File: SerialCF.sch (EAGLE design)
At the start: 17 parts, among them IC1 XR-16C550P, T1 BC547, T2 BC547

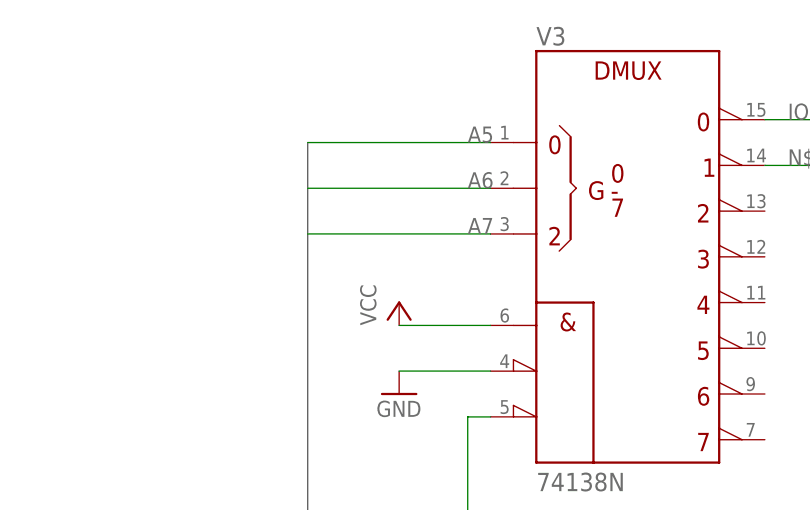
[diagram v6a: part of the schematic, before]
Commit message: Use upper Bits to Address IO devices.
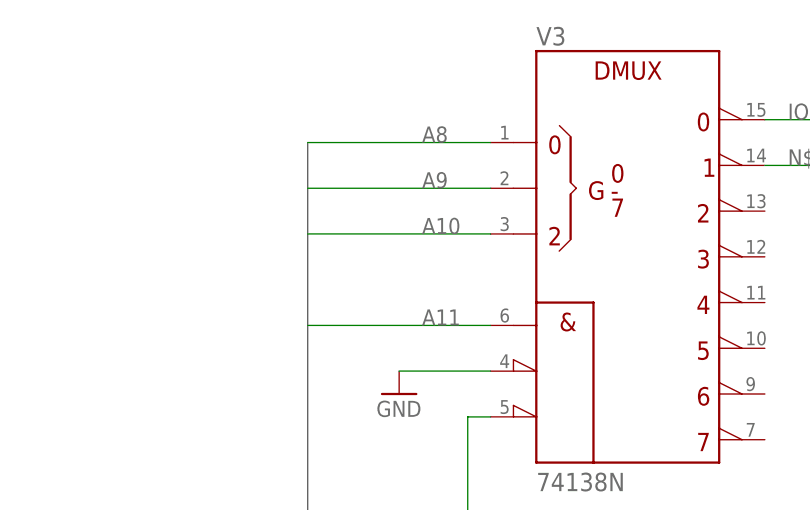
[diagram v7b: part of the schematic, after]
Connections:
- net A10: now also V31.C
- net A11: now also V31.G1
- net A5: no longer V31.A
- net A6: no longer V31.B
- net A7: no longer V31.C
- net A8: now also V31.A
- net A9: now also V31.B
- net VCC: no longer V31.G1
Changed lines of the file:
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@@
 <part name="GND9" library="supply1" deviceset="GND" device=""/>
 <part name="V3" library="74ttl-din" deviceset="74*138" device="N"/>
-<part name="P+12" library="supply1" deviceset="VCC" device=""/>
 <part name="GND13" library="supply1" deviceset="GND" device=""/>
 <part name="T2" library="transistor" deviceset="BC547" device=""/>
@@
 <instance part="V3" gate="/+UB" x="17.78" y="96.52"/>
 <instance part="V3" gate="/-UB" x="17.78" y="86.36"/>
-<instance part="P+12" gate="VCC" x="86.36" y="132.08"/>
 <instance part="GND13" gate="1" x="86.36" y="121.92"/>
 <instance part="T2" gate="G$1" x="111.76" y="-15.24"/>
@@
 <pinref part="JP1" gate="A" pin="A7"/>
 <wire x1="66.04" y1="48.26" x2="76.2" y2="48.26" width="0.1524" layer="91"/>
-</segment>
-<segment>
-<pinref part="V3" gate="1" pin="C"/>
-<wire x1="96.52" y1="139.7" x2="76.2" y2="139.7" width="0.1524" layer="91"/>
-<label x="93.98" y="139.7" size="1.778" layer="95"/>
 </segment>
 </net>
@@
 <pinref part="P+1" gate="VCC" pin="VCC"/>
 <pinref part="V3" gate="/+UB" pin="+UB"/>
-</segment>
-<segment>
-<pinref part="P+12" gate="VCC" pin="VCC"/>
-<pinref part="V3" gate="1" pin="G1"/>
-<wire x1="86.36" y1="129.54" x2="96.52" y2="129.54" width="0.1524" layer="91"/>
 </segment>
 <segment>
@@
 <wire x1="66.04" y1="53.34" x2="76.2" y2="53.34" width="0.1524" layer="91"/>
 </segment>
-<segment>
-<pinref part="V3" gate="1" pin="A"/>
-<wire x1="96.52" y1="149.86" x2="76.2" y2="149.86" width="0.1524" layer="91"/>
-<label x="93.98" y="149.86" size="1.778" layer="95"/>
-</segment>
 </net>
 <net name="A6" class="0">
@@
 <wire x1="266.7" y1="68.58" x2="266.7" y2="73.66" width="0.1524" layer="91"/>
 </segment>
-<segment>
-<pinref part="V3" gate="1" pin="B"/>
-<wire x1="96.52" y1="144.78" x2="76.2" y2="144.78" width="0.1524" layer="91"/>
-<label x="93.98" y="144.78" size="1.778" layer="95"/>
-</segment>
 </net>
 <net name="A8" class="0">
@@
 <wire x1="66.04" y1="45.72" x2="76.2" y2="45.72" width="0.1524" layer="91"/>
 </segment>
+<segment>
+<pinref part="V3" gate="1" pin="A"/>
+<wire x1="76.2" y1="149.86" x2="96.52" y2="149.86" width="0.1524" layer="91"/>
+<label x="88.9" y="149.86" size="1.778" layer="95"/>
+</segment>
 </net>
 <net name="A9" class="0">
@@
 <wire x1="66.04" y1="43.18" x2="76.2" y2="43.18" width="0.1524" layer="91"/>
 </segment>
+<segment>
+<pinref part="V3" gate="1" pin="B"/>
+<wire x1="76.2" y1="144.78" x2="96.52" y2="144.78" width="0.1524" layer="91"/>
+<label x="88.9" y="144.78" size="1.778" layer="95"/>
+</segment>
 </net>
 <net name="A10" class="0">
@@
 <wire x1="66.04" y1="40.64" x2="76.2" y2="40.64" width="0.1524" layer="91"/>
 </segment>
+<segment>
+<pinref part="V3" gate="1" pin="C"/>
+<wire x1="76.2" y1="139.7" x2="96.52" y2="139.7" width="0.1524" layer="91"/>
+<label x="88.9" y="139.7" size="1.778" layer="95"/>
+</segment>
 </net>
 <net name="A11" class="0">
@@
 <wire x1="66.04" y1="38.1" x2="76.2" y2="38.1" width="0.1524" layer="91"/>
 </segment>
-</net>
+<segment>
+<pinref part="V3" gate="1" pin="G1"/>
+<wire x1="76.2" y1="129.54" x2="96.52" y2="129.54" width="0.1524" layer="91"/>
+<label x="88.9" y="129.54" size="1.778" layer="95"/>
+</segment>
+</net>

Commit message: Use LS version for serialCF
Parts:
- removed V3: 74138N, 74ttl-din:74138N
- added IC2: 74LS138N, 74xx-eu:74LS138N
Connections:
- net A10: now also IC2A.C; no longer V31.C
- net A11: now also IC2A.G1; no longer V31.G1
- net A8: now also IC2A.A; no longer V31.A
- net A9: now also IC2A.B; no longer V31.B
- net GND: now also IC2P.GND; no longer V3/-UB.-UB, V31.!G2A
- net IOCS1: no longer V31.Y0
- net N$4: now also IC2A.Y1; no longer V31.Y1
- net N$5: no longer V31.!G2B
- net VCC: now also IC2P.VCC; no longer V3/+UB.+UB
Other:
- note removed: "A7 = 0 A6 = 0"
- note removed: "A7 = 0 A6 = 1"
- moved on the sheet: C4
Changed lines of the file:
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@@
 <part name="P+11" library="supply1" deviceset="VCC" device=""/>
 <part name="GND9" library="supply1" deviceset="GND" device=""/>
-<part name="V3" library="74ttl-din" deviceset="74*138" device="N"/>
 <part name="GND13" library="supply1" deviceset="GND" device=""/>
 <part name="T2" library="transistor" deviceset="BC547" device=""/>
@@
 <part name="P+13" library="supply1" deviceset="VCC" device=""/>
 <part name="GND14" library="supply1" deviceset="GND" device=""/>
+<part name="IC2" library="74xx-eu" deviceset="74*138" device="N" technology="LS"/>
 </parts>
 <sheets>
 <sheet>
 <plain>
-<text x="157.48" y="55.88" size="1.778" layer="91">A7 = 0
-A6 = 1</text>
-<text x="281.94" y="53.34" size="1.778" layer="91">A7 = 0
-A6 = 0</text>
 </plain>
 <instances>
@@
 <instance part="P+7" gate="VCC" x="314.96" y="43.18"/>
 <instance part="GND6" gate="1" x="314.96" y="30.48"/>
-<instance part="C4" gate="G$1" x="223.52" y="111.76"/>
-<instance part="P+11" gate="VCC" x="223.52" y="116.84"/>
-<instance part="GND9" gate="1" x="223.52" y="104.14"/>
-<instance part="V3" gate="1" x="111.76" y="137.16"/>
-<instance part="V3" gate="/+UB" x="17.78" y="96.52"/>
-<instance part="V3" gate="/-UB" x="17.78" y="86.36"/>
-<instance part="GND13" gate="1" x="86.36" y="121.92"/>
+<instance part="C4" gate="G$1" x="297.18" y="63.5"/>
+<instance part="P+11" gate="VCC" x="297.18" y="68.58"/>
+<instance part="GND9" gate="1" x="297.18" y="55.88"/>
+<instance part="GND13" gate="1" x="86.36" y="132.08"/>
 <instance part="T2" gate="G$1" x="111.76" y="-15.24"/>
 <instance part="R5" gate="G$1" x="101.6" y="-15.24"/>
@@
 <instance part="P+13" gate="VCC" x="114.3" y="2.54"/>
 <instance part="GND14" gate="1" x="114.3" y="-22.86"/>
+<instance part="IC2" gate="A" x="111.76" y="142.24"/>
+<instance part="IC2" gate="P" x="17.78" y="91.44"/>
 </instances>
 <busses>
@@
 </segment>
 <segment>
-<pinref part="P+1" gate="VCC" pin="VCC"/>
-<pinref part="V3" gate="/+UB" pin="+UB"/>
-</segment>
-<segment>
 <pinref part="R6" gate="G$1" pin="2"/>
 <pinref part="P+13" gate="VCC" pin="VCC"/>
+</segment>
+<segment>
+<pinref part="P+1" gate="VCC" pin="VCC"/>
+<pinref part="IC2" gate="P" pin="VCC"/>
 </segment>
 </net>
@@
 </segment>
 <segment>
-<pinref part="GND3" gate="1" pin="GND"/>
-<pinref part="V3" gate="/-UB" pin="-UB"/>
-</segment>
-<segment>
 <pinref part="T2" gate="G$1" pin="E"/>
 <pinref part="GND14" gate="1" pin="GND"/>
 </segment>
 <segment>
-<pinref part="V3" gate="1" pin="!G2A"/>
 <pinref part="GND13" gate="1" pin="GND"/>
-<wire x1="96.52" y1="124.46" x2="86.36" y2="124.46" width="0.1524" layer="91"/>
+<wire x1="96.52" y1="134.62" x2="86.36" y2="134.62" width="0.1524" layer="91"/>
+</segment>
+<segment>
+<pinref part="GND3" gate="1" pin="GND"/>
+<pinref part="IC2" gate="P" pin="GND"/>
 </segment>
 </net>
@@
 <pinref part="SV2" gate="G$1" pin="37"/>
 <label x="271.78" y="2.54" size="1.778" layer="95"/>
-<wire x1="276.86" y1="2.54" x2="266.7" y2="2.54" width="0.1524" layer="91"/>
-<pinref part="V3" gate="1" pin="Y0"/>
-<wire x1="127" y1="152.4" x2="266.7" y2="152.4" width="0.1524" layer="91"/>
-<wire x1="266.7" y1="2.54" x2="266.7" y2="152.4" width="0.1524" layer="91"/>
+<wire x1="276.86" y1="2.54" x2="264.16" y2="2.54" width="0.1524" layer="91"/>
+<wire x1="124.46" y1="149.86" x2="264.16" y2="149.86" width="0.1524" layer="91"/>
+<wire x1="264.16" y1="2.54" x2="264.16" y2="149.86" width="0.1524" layer="91"/>
 <label x="129.54" y="152.4" size="1.778" layer="95"/>
 </segment>
@@
 <wire x1="66.04" y1="50.8" x2="76.2" y2="50.8" width="0.1524" layer="91"/>
 </segment>
-<segment>
-<wire x1="266.7" y1="68.58" x2="266.7" y2="73.66" width="0.1524" layer="91"/>
-</segment>
 </net>
 <net name="A8" class="0">
@@
 </segment>
 <segment>
-<pinref part="V3" gate="1" pin="A"/>
 <wire x1="76.2" y1="149.86" x2="96.52" y2="149.86" width="0.1524" layer="91"/>
 <label x="88.9" y="149.86" size="1.778" layer="95"/>
+<pinref part="IC2" gate="A" pin="A"/>
 </segment>
 </net>
@@
 </segment>
 <segment>
-<pinref part="V3" gate="1" pin="B"/>
-<wire x1="76.2" y1="144.78" x2="96.52" y2="144.78" width="0.1524" layer="91"/>
-<label x="88.9" y="144.78" size="1.778" layer="95"/>
+<pinref part="IC2" gate="A" pin="B"/>
+<wire x1="96.52" y1="147.32" x2="76.2" y2="147.32" width="0.1524" layer="91"/>
 </segment>
 </net>
@@
 </segment>
 <segment>
-<pinref part="V3" gate="1" pin="C"/>
-<wire x1="76.2" y1="139.7" x2="96.52" y2="139.7" width="0.1524" layer="91"/>
-<label x="88.9" y="139.7" size="1.778" layer="95"/>
+<pinref part="IC2" gate="A" pin="C"/>
+<wire x1="96.52" y1="144.78" x2="76.2" y2="144.78" width="0.1524" layer="91"/>
 </segment>
 </net>
@@
 </segment>
 <segment>
-<pinref part="V3" gate="1" pin="G1"/>
-<wire x1="76.2" y1="129.54" x2="96.52" y2="129.54" width="0.1524" layer="91"/>
-<label x="88.9" y="129.54" size="1.778" layer="95"/>
+<pinref part="IC2" gate="A" pin="G1"/>
+<wire x1="96.52" y1="137.16" x2="76.2" y2="137.16" width="0.1524" layer="91"/>
 </segment>
 </net>
@@
 <wire x1="152.4" y1="27.94" x2="139.7" y2="27.94" width="0.1524" layer="91"/>
 <wire x1="139.7" y1="27.94" x2="139.7" y2="147.32" width="0.1524" layer="91"/>
-<pinref part="V3" gate="1" pin="Y1"/>
-<wire x1="139.7" y1="147.32" x2="127" y2="147.32" width="0.1524" layer="91"/>
+<wire x1="139.7" y1="147.32" x2="124.46" y2="147.32" width="0.1524" layer="91"/>
 <label x="129.54" y="147.32" size="1.778" layer="95"/>
+<pinref part="IC2" gate="A" pin="Y1"/>
 </segment>
 </net>
 <net name="N$5" class="0">
 <segment>
-<pinref part="V3" gate="1" pin="!G2B"/>
-<wire x1="96.52" y1="119.38" x2="93.98" y2="119.38" width="0.1524" layer="91"/>
-<wire x1="93.98" y1="119.38" x2="93.98" y2="12.7" width="0.1524" layer="91"/>
+<wire x1="96.52" y1="132.08" x2="93.98" y2="132.08" width="0.1524" layer="91"/>
+<wire x1="93.98" y1="132.08" x2="93.98" y2="12.7" width="0.1524" layer="91"/>
 <pinref part="JP1" gate="A" pin="!IOREQ"/>
 <wire x1="66.04" y1="12.7" x2="93.98" y2="12.7" width="0.1524" layer="91"/>
@@
 </schematic>
 </drawing>
-<compatibility>
-<note version="6.3" minversion="6.2.2" severity="warning">
-Since Version 6.2.2 text objects can contain more than one line,
-which will not be processed correctly with this version.
-</note>
-</compatibility>
 </eagle>
